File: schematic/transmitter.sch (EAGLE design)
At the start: 5 parts

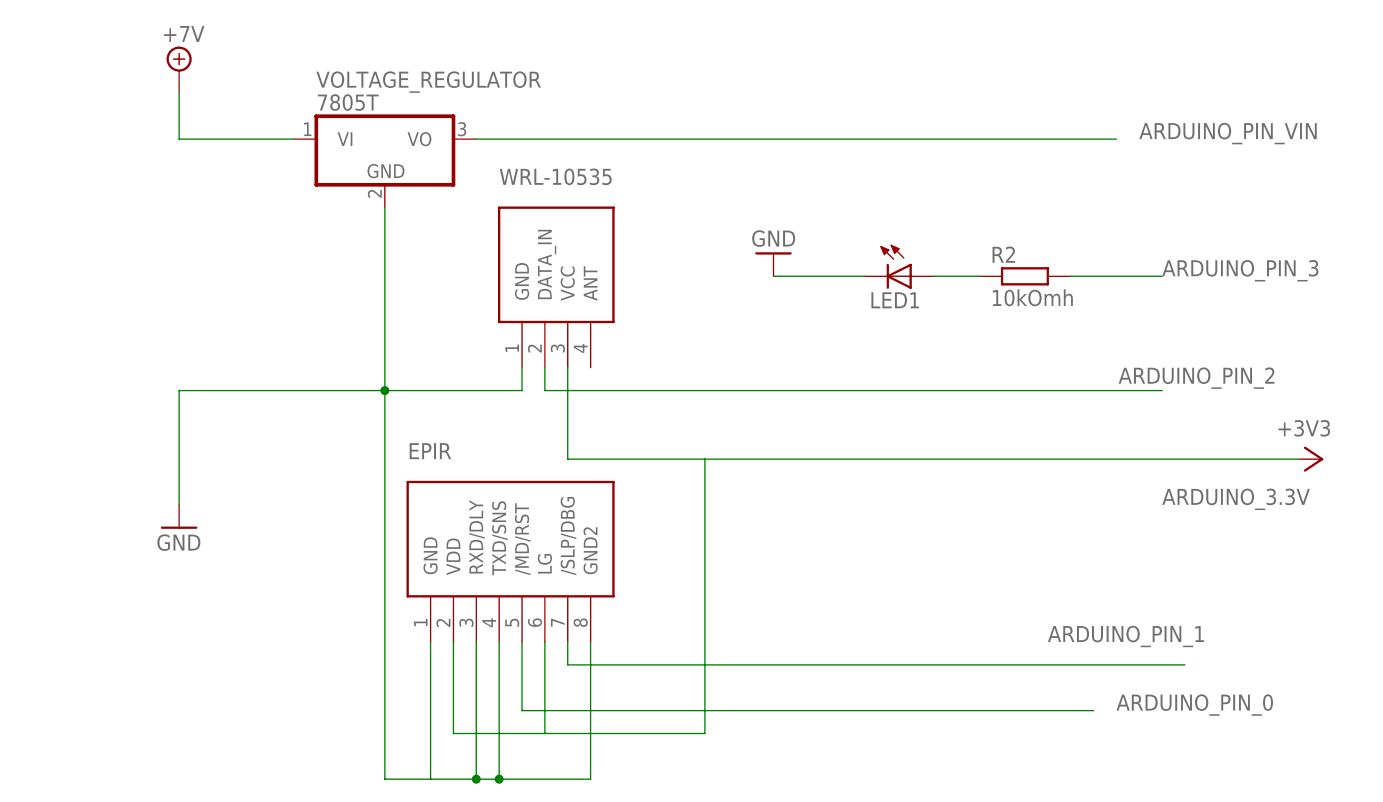
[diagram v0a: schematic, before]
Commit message: updated schematic: added attiny85
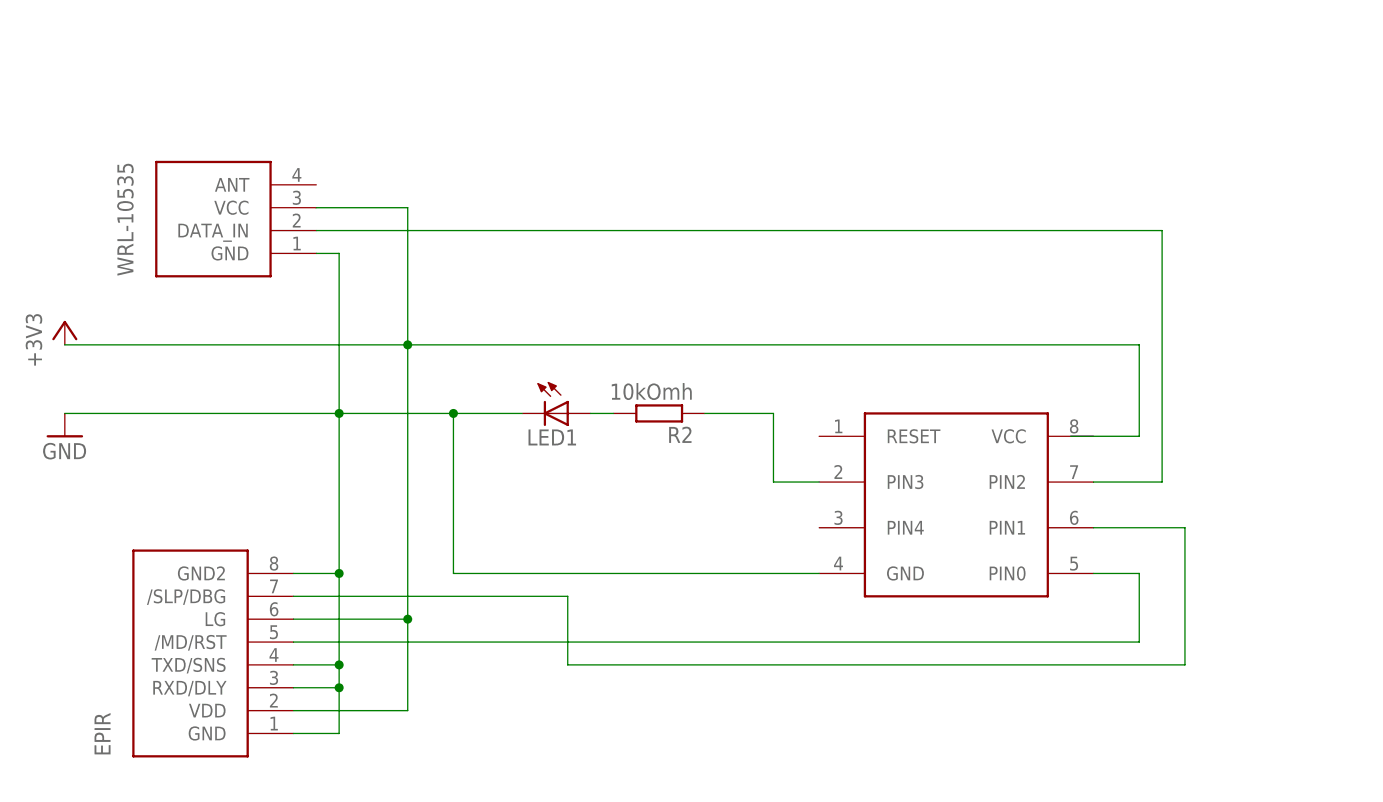
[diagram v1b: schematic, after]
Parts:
- removed VOLTAGE_REGULATOR: 7805T, linear:7805T
- added U$3: ATTINY85, stuff:ATTINY85
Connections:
- net ARDUINO_3.3V renamed +3V3
- removed net +7V: VOLTAGE_REGULATOR.VI
- removed net ARDUINO_PIN_3: R2.2
- removed net ARDUINO_PIN_VIN: VOLTAGE_REGULATOR.VO
- removed net N$4: U$1.GND, U$1.GND2, U$1.RXD/DLY, U$1.TXD/SNS
- new net N$3: LED1.A, R2.2
- net ARDUINO_PIN_0: now also U$3.PIN0
- net ARDUINO_PIN_1: now also U$3.PIN1
- net ARDUINO_PIN_2: now also U$3.PIN2
- net GND: now also U$1.GND, U$1.GND2, U$1.RXD/DLY, U$1.TXD/SNS, U$3.GND; no longer VOLTAGE_REGULATOR.GND
- net N$2: now also U$3.PIN3; no longer LED1.A
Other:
- moved on the sheet: LED1, R2
